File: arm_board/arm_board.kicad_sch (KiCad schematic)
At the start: 34 parts, among them J1 Conn_01x04_Pin, J10 RJ45_LED_Shielded, J11 Conn_01x02_Pin, J12 Conn_01x03_Pin, J2 Conn_01x03_Pin, J3 Conn_01x02_Pin, J5 Conn_01x03_Pin, J6 Conn_01x03_Pin, J7 Conn_01x03_Pin, J9 Conn_01x02_Pin, Q3 BSS138, SW10 SW_Push, SW11 SW_Push, SW12 SW_Push, SW13 SW_Push, SW14 SW_Push, SW15 SW_SPDT, SW16 SW_SPDT, SW9 SW_Push, U1 SN65HVD232

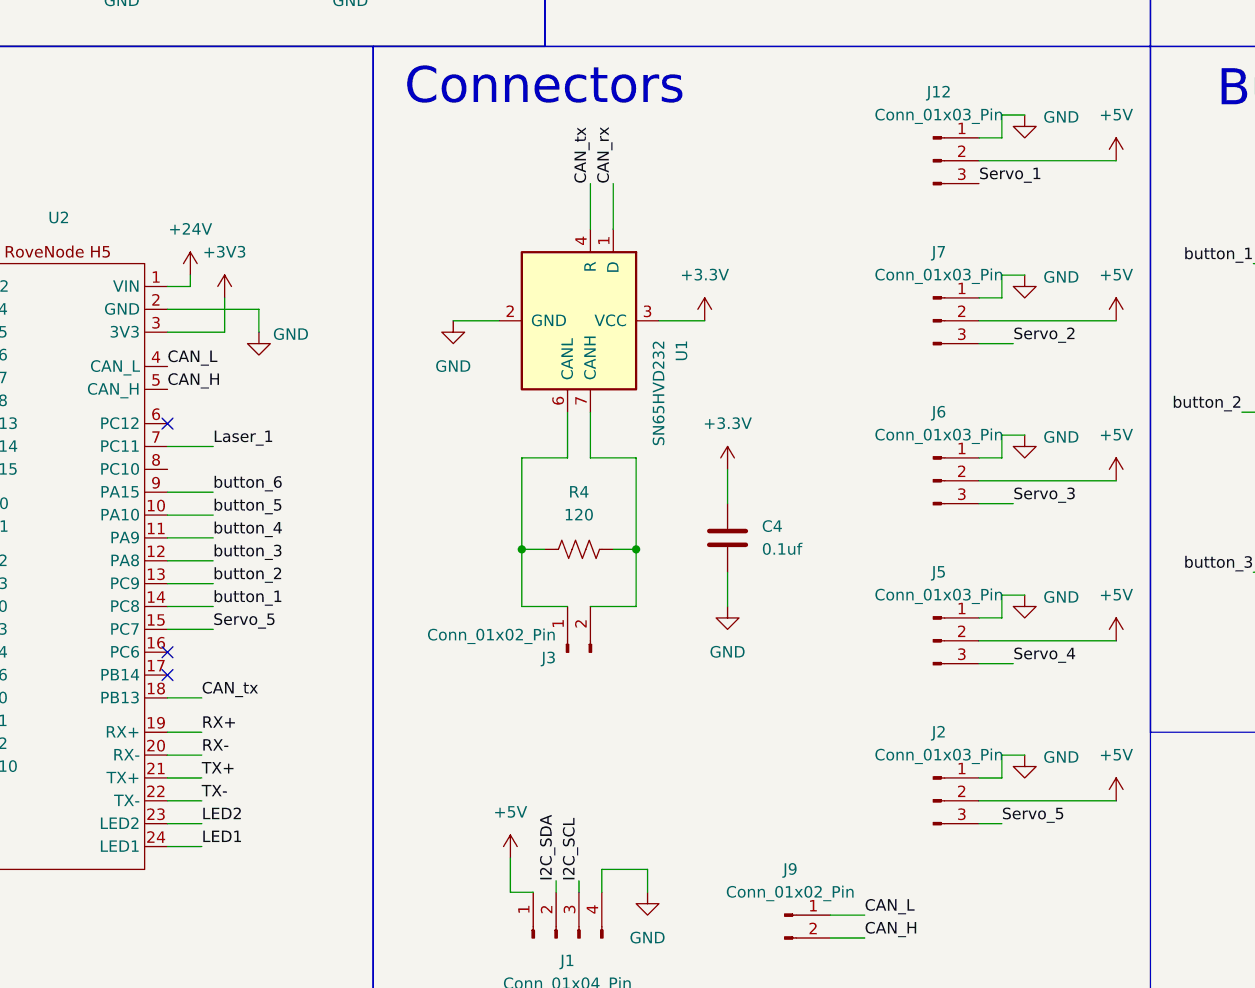
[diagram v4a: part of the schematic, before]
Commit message: updated the button footprints
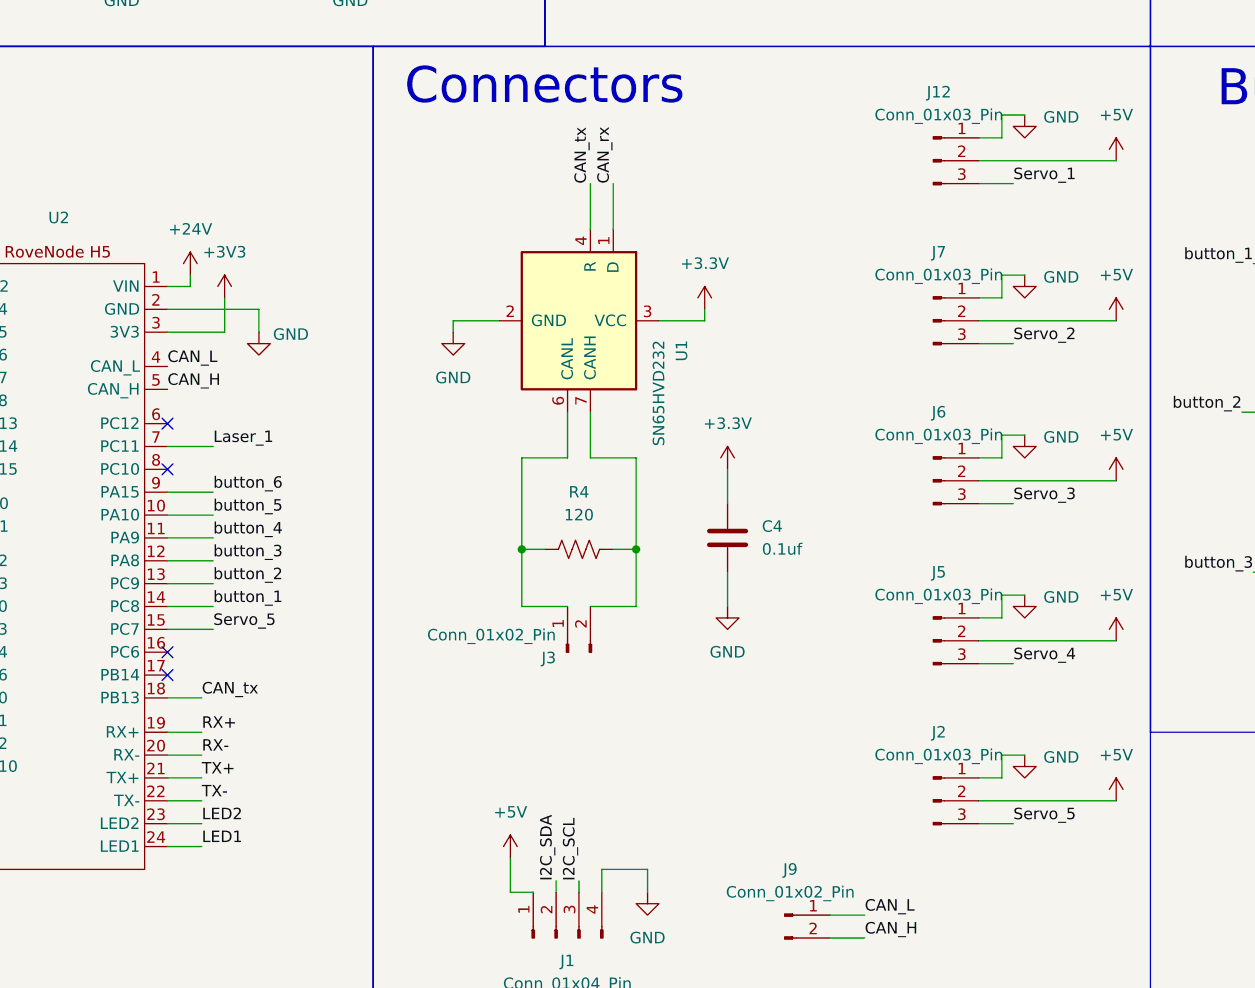
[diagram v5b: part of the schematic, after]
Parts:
- D4: footprint (none) -> LED_SMD:LED_0603_1608Metric_Pad1.05x0.95mm_HandSolder
- J3: footprint Oscillator:Oscillator_SMD_OCXO_ConnorWinfield_OH300 -> Connector_JST:JST_SH_SM02B-SRSS-TB_1x02-1MP_P1.00mm_Horizontal
- R4, R5: footprint Package_LCC:PLCC-84_29.3x29.3mm_P1.27mm -> Resistor_SMD:R_0603_1608Metric_Pad0.98x0.95mm_HandSolder
- SW10, SW11, SW13, SW14, SW9: footprint Button_Switch_THT:SW_Slide_SPDT_Angled_CK_OS102011MA1Q -> Button_Switch_SMD:SW_SPST_TL3305A
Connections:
- no-connect marks 16 -> 17
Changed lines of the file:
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@@
 	)
 	(no_connect
+		(at 63.5 135.89)
+	)
+	(no_connect
 		(at 39.37 142.24)
 	)
@@
 	(wire
 		(pts
-			(xy 123.19 119.38) (xy 118.11 119.38)
-		)
-		(stroke
-			(width 0)
-			(type default)
-		)
-	)
-	(wire
-		(pts
 			(xy 156.21 152.4) (xy 156.21 149.86)
 		)
@@
 	(wire
 		(pts
+			(xy 123.19 118.11) (xy 123.19 119.38)
+		)
+		(stroke
+			(width 0)
+			(type default)
+		)
+	)
+	(wire
+		(pts
 			(xy 143.51 31.75) (xy 149.86 31.75)
 		)
@@
 	(wire
 		(pts
-			(xy 100.33 119.38) (xy 95.25 119.38)
-		)
-		(stroke
-			(width 0)
-			(type default)
-		)
-	)
-	(wire
-		(pts
 			(xy 196.85 147.32) (xy 200.66 147.32)
 		)
@@
 	(wire
 		(pts
+			(xy 95.25 120.65) (xy 95.25 119.38)
+		)
+		(stroke
+			(width 0)
+			(type default)
+		)
+	)
+	(wire
+		(pts
 			(xy 156.21 99.06) (xy 156.21 96.52)
 		)
@@
 	(wire
 		(pts
-			(xy 153.67 175.26) (xy 156.21 175.26)
+			(xy 153.67 175.26) (xy 157.48 175.26)
 		)
 		(stroke
@@
 	(wire
 		(pts
+			(xy 95.25 119.38) (xy 100.33 119.38)
+		)
+		(stroke
+			(width 0)
+			(type default)
+		)
+	)
+	(wire
+		(pts
 			(xy 184.15 147.32) (xy 186.69 147.32)
 		)
@@
 	(wire
 		(pts
+			(xy 123.19 119.38) (xy 118.11 119.38)
+		)
+		(stroke
+			(width 0)
+			(type default)
+		)
+	)
+	(wire
+		(pts
 			(xy 156.21 114.3) (xy 158.75 114.3)
 		)
@@
 	(wire
 		(pts
+			(xy 157.48 104.14) (xy 153.67 104.14)
+		)
+		(stroke
+			(width 0)
+			(type default)
+		)
+	)
+	(wire
+		(pts
 			(xy 241.3 139.7) (xy 241.3 142.24)
 		)
@@
 	)
 	(label "Servo_1"
-		(at 153.67 104.14 0)
+		(at 157.48 104.14 0)
 		(effects
 			(font
@@
 	)
 	(label "Servo_5"
-		(at 156.21 175.26 0)
+		(at 157.48 175.26 0)
 		(effects
 			(font
@@
 			)
 		)
-		(property "Footprint" "Oscillator:Oscillator_SMD_OCXO_ConnorWinfield_OH300"
+		(property "Footprint" "Connector_JST:JST_SH_SM02B-SRSS-TB_1x02-1MP_P1.00mm_Horizontal"
 			(at 107.95 156.21 0)
 			(hide yes)
@@
 	(symbol
 		(lib_id "power:GND")
-		(at 95.25 119.38 0)
+		(at 95.25 120.65 0)
 		(unit 1)
 		(body_style 1)
@@
 		(fields_autoplaced yes)
 		(property "Reference" "#PWR03"
-			(at 95.25 125.73 0)
+			(at 95.25 127 0)
 			(hide yes)
 			(show_name no)
@@
 		)
 		(property "Value" "GND"
-			(at 95.25 124.46 0)
+			(at 95.25 125.73 0)
 			(show_name no)
 			(do_not_autoplace no)
@@
 		)
 		(property "Footprint" "Package_SO:SOIC-8_3.9x4.9mm_P1.27mm"
-			(at 95.25 119.38 0)
+			(at 95.25 120.65 0)
 			(hide yes)
 			(show_name no)
@@
 		)
 		(property "Datasheet" ""
-			(at 95.25 119.38 0)
+			(at 95.25 120.65 0)
 			(hide yes)
 			(show_name no)
@@
 		)
 		(property "Description" "Power symbol creates a global label with name \"GND\" , ground"
-			(at 95.25 119.38 0)
+			(at 95.25 120.65 0)
 			(hide yes)
 			(show_name no)
@@
 			)
 		)
-		(property "Footprint" "Button_Switch_THT:SW_Slide_SPDT_Angled_CK_OS102011MA1Q"
+		(property "Footprint" "Button_Switch_SMD:SW_SPST_TL3305A"
 			(at 223.52 142.24 0)
 			(hide yes)
@@
 			)
 		)
-		(property "Footprint" "Package_LCC:PLCC-84_29.3x29.3mm_P1.27mm"
+		(property "Footprint" "Resistor_SMD:R_0603_1608Metric_Pad0.98x0.95mm_HandSolder"
 			(at 275.336 142.494 90)
 			(hide yes)
@@
 			)
 		)
-		(property "Footprint" "Button_Switch_THT:SW_Slide_SPDT_Angled_CK_OS102011MA1Q"
+		(property "Footprint" "Button_Switch_SMD:SW_SPST_TL3305A"
 			(at 223.52 123.19 0)
 			(hide yes)
@@
 			)
 		)
-		(property "Footprint" "Button_Switch_THT:SW_Slide_SPDT_Angled_CK_OS102011MA1Q"
+		(property "Footprint" "Button_Switch_SMD:SW_SPST_TL3305A"
 			(at 191.77 142.24 0)
 			(hide yes)
@@
 	(symbol
 		(lib_id "power:+3.3V")
-		(at 123.19 119.38 0)
+		(at 123.19 118.11 0)
 		(unit 1)
 		(body_style 1)
@@
 		(fields_autoplaced yes)
 		(property "Reference" "#PWR09"
-			(at 123.19 123.19 0)
+			(at 123.19 121.92 0)
 			(hide yes)
 			(show_name no)
@@
 		)
 		(property "Value" "+3.3V"
-			(at 123.19 114.3 0)
+			(at 123.19 113.03 0)
 			(show_name no)
 			(do_not_autoplace no)
@@
 		)
 		(property "Footprint" "Package_DFN_QFN:Diodes_UDFN3810-9_TYPE_B"
-			(at 123.19 119.38 0)
+			(at 123.19 118.11 0)
 			(hide yes)
 			(show_name no)
@@
 		)
 		(property "Datasheet" ""
-			(at 123.19 119.38 0)
+			(at 123.19 118.11 0)
 			(hide yes)
 			(show_name no)
@@
 		)
 		(property "Description" "Power symbol creates a global label with name \"+3.3V\""
-			(at 123.19 119.38 0)
+			(at 123.19 118.11 0)
 			(hide yes)
 			(show_name no)
@@
 			)
 		)
-		(property "Footprint" ""
+		(property "Footprint" "LED_SMD:LED_0603_1608Metric_Pad1.05x0.95mm_HandSolder"
 			(at 274.32 132.08 0)
 			(hide yes)
@@
 			)
 		)
-		(property "Footprint" "Package_LCC:PLCC-84_29.3x29.3mm_P1.27mm"
+		(property "Footprint" "Resistor_SMD:R_0603_1608Metric_Pad0.98x0.95mm_HandSolder"
 			(at 108.966 145.796 90)
 			(hide yes)
@@
 			)
 		)
-		(property "Footprint" "Button_Switch_THT:SW_Slide_SPDT_Angled_CK_OS102011MA1Q"
+		(property "Footprint" "Button_Switch_SMD:SW_SPST_TL3305A"
 			(at 191.77 124.46 0)
 			(hide yes)
@@
 			)
 		)
-		(property "Footprint" "Button_Switch_THT:SW_Slide_SPDT_Angled_CK_OS102011MA1Q"
+		(property "Footprint" "Button_Switch_SMD:SW_SPST_TL3305A"
 			(at 191.77 107.95 0)
 			(hide yes)

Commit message: updated footprints
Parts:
- J1: footprint Connector_Audio:Jack_XLR_Neutrik_NC3FAAH_Horizontal -> Connector_JST:JST_PH_S4B-PH-K_1x04_P2.00mm_Horizontal
- J11: footprint Connector_JST:JST_SH_SM02B-SRSS-TB_1x02-1MP_P1.00mm_Horizontal -> Connector_JST:JST_PH_S2B-PH-K_1x02_P2.00mm_Horizontal
- J12, J2, J5, J6, J7: footprint Connector_JST:JST_SH_SM03B-SRSS-TB_1x03-1MP_P1.00mm_Horizontal -> Connector_JST:JST_PH_S3B-PH-K_1x03_P2.00mm_Horizontal
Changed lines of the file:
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@@
 			)
 		)
-		(property "Footprint" "Connector_JST:JST_SH_SM03B-SRSS-TB_1x03-1MP_P1.00mm_Horizontal"
+		(property "Footprint" "Connector_JST:JST_PH_S3B-PH-K_1x03_P2.00mm_Horizontal"
 			(at 148.59 154.94 0)
 			(hide yes)
@@
 			)
 		)
-		(property "Footprint" "Connector_JST:JST_SH_SM03B-SRSS-TB_1x03-1MP_P1.00mm_Horizontal"
+		(property "Footprint" "Connector_JST:JST_PH_S3B-PH-K_1x03_P2.00mm_Horizontal"
 			(at 148.59 119.38 0)
 			(hide yes)
@@
 			)
 		)
-		(property "Footprint" "Connector_JST:JST_SH_SM02B-SRSS-TB_1x02-1MP_P1.00mm_Horizontal"
+		(property "Footprint" "Connector_JST:JST_PH_S2B-PH-K_1x02_P2.00mm_Horizontal"
 			(at 209.55 35.56 0)
 			(hide yes)
@@
 			)
 		)
-		(property "Footprint" "Connector_JST:JST_SH_SM03B-SRSS-TB_1x03-1MP_P1.00mm_Horizontal"
+		(property "Footprint" "Connector_JST:JST_PH_S3B-PH-K_1x03_P2.00mm_Horizontal"
 			(at 148.59 137.16 0)
 			(hide yes)
@@
 			)
 		)
-		(property "Footprint" "Connector_Audio:Jack_XLR_Neutrik_NC3FAAH_Horizontal"
+		(property "Footprint" "Connector_JST:JST_PH_S4B-PH-K_1x04_P2.00mm_Horizontal"
 			(at 106.68 187.96 0)
 			(hide yes)
@@
 			)
 		)
-		(property "Footprint" "Connector_JST:JST_SH_SM03B-SRSS-TB_1x03-1MP_P1.00mm_Horizontal"
+		(property "Footprint" "Connector_JST:JST_PH_S3B-PH-K_1x03_P2.00mm_Horizontal"
 			(at 148.59 101.6 0)
 			(hide yes)
@@
 			)
 		)
-		(property "Footprint" "Connector_JST:JST_SH_SM03B-SRSS-TB_1x03-1MP_P1.00mm_Horizontal"
+		(property "Footprint" "Connector_JST:JST_PH_S3B-PH-K_1x03_P2.00mm_Horizontal"
 			(at 148.59 172.72 0)
 			(hide yes)

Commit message: updated footprints ... again
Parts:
- J3, J9: footprint Connector_JST:JST_SH_SM02B-SRSS-TB_1x02-1MP_P1.00mm_Horizontal -> Connector_JST:JST_PH_S2B-PH-K_1x02_P2.00mm_Horizontal
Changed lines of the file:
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@@
 			)
 		)
-		(property "Footprint" "Connector_JST:JST_SH_SM02B-SRSS-TB_1x02-1MP_P1.00mm_Horizontal"
+		(property "Footprint" "Connector_JST:JST_PH_S2B-PH-K_1x02_P2.00mm_Horizontal"
 			(at 107.95 156.21 0)
 			(hide yes)
@@
 			)
 		)
-		(property "Footprint" "Connector_JST:JST_SH_SM02B-SRSS-TB_1x02-1MP_P1.00mm_Horizontal"
+		(property "Footprint" "Connector_JST:JST_PH_S2B-PH-K_1x02_P2.00mm_Horizontal"
 			(at 132.08 185.42 0)
 			(hide yes)

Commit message: changed pin assignments
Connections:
- net button_6: now also U2.16 (PC6); no longer U2.9 (PA15)
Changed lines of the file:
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@@
+	)
+	(no_connect
+		(at 63.5 138.43)
 	)
 	(no_connect
@@
 	)
 	(no_connect
-		(at 63.5 156.21)
-	)
-	(no_connect
 		(at 39.37 135.89)
 	)
@@
 	(wire
 		(pts
-			(xy 68.58 138.43) (xy 63.5 138.43)
-		)
-		(stroke
-			(width 0)
-			(type default)
-		)
-	)
-	(wire
-		(pts
 			(xy 115.57 134.62) (xy 115.57 151.13)
 		)
@@
 		(pts
 			(xy 58.42 78.74) (xy 58.42 77.47)
+		)
+		(stroke
+			(width 0)
+			(type default)
+		)
+	)
+	(wire
+		(pts
+			(xy 68.58 156.21) (xy 63.5 156.21)
 		)
 		(stroke
@@
 		)
 	)
-	(label "button_6"
-		(at 68.58 138.43 0)
-		(effects
-			(font
-				(size 1.27 1.27)
-			)
-			(justify left bottom)
-		)
-	)
 	(label "RX+"
 		(at 133.35 55.88 270)
@@
 		(effects
 			(font
+				(size 1.27 1.27)
+			)
+			(justify left bottom)
+		)
+	)
+	(label "button_6"
+		(at 68.58 156.21 0)
+		(effects
+			(font
